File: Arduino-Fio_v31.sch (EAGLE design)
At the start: 56 parts, among them U1 MCP73831, U5 ATMEGA32U4, U6 MIC5219-3.3, X1 MJ4435-R1503_03, X2 USB_MICROB_PLUGCONN-11752, Y2 8MHz

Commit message: V 0.11 now with SD card slot
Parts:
- added U$3: MICROSD, adafruit:MICROSD
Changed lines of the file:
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@@
 <part name="PAD5" library="wirepad" deviceset="WIREPAD" device="SMD1,27-254"/>
 <part name="PAD6" library="wirepad" deviceset="WIREPAD" device="SMD1,27-254"/>
+<part name="U$3" library="adafruit" deviceset="MICROSD" device=""/>
 </parts>
 <sheets>
@@
 <instance part="PAD5" gate="G$1" x="-33.02" y="104.14"/>
 <instance part="PAD6" gate="G$1" x="-33.02" y="96.52"/>
+<instance part="U$3" gate="G$1" x="307.34" y="109.22"/>
 </instances>
 <busses>

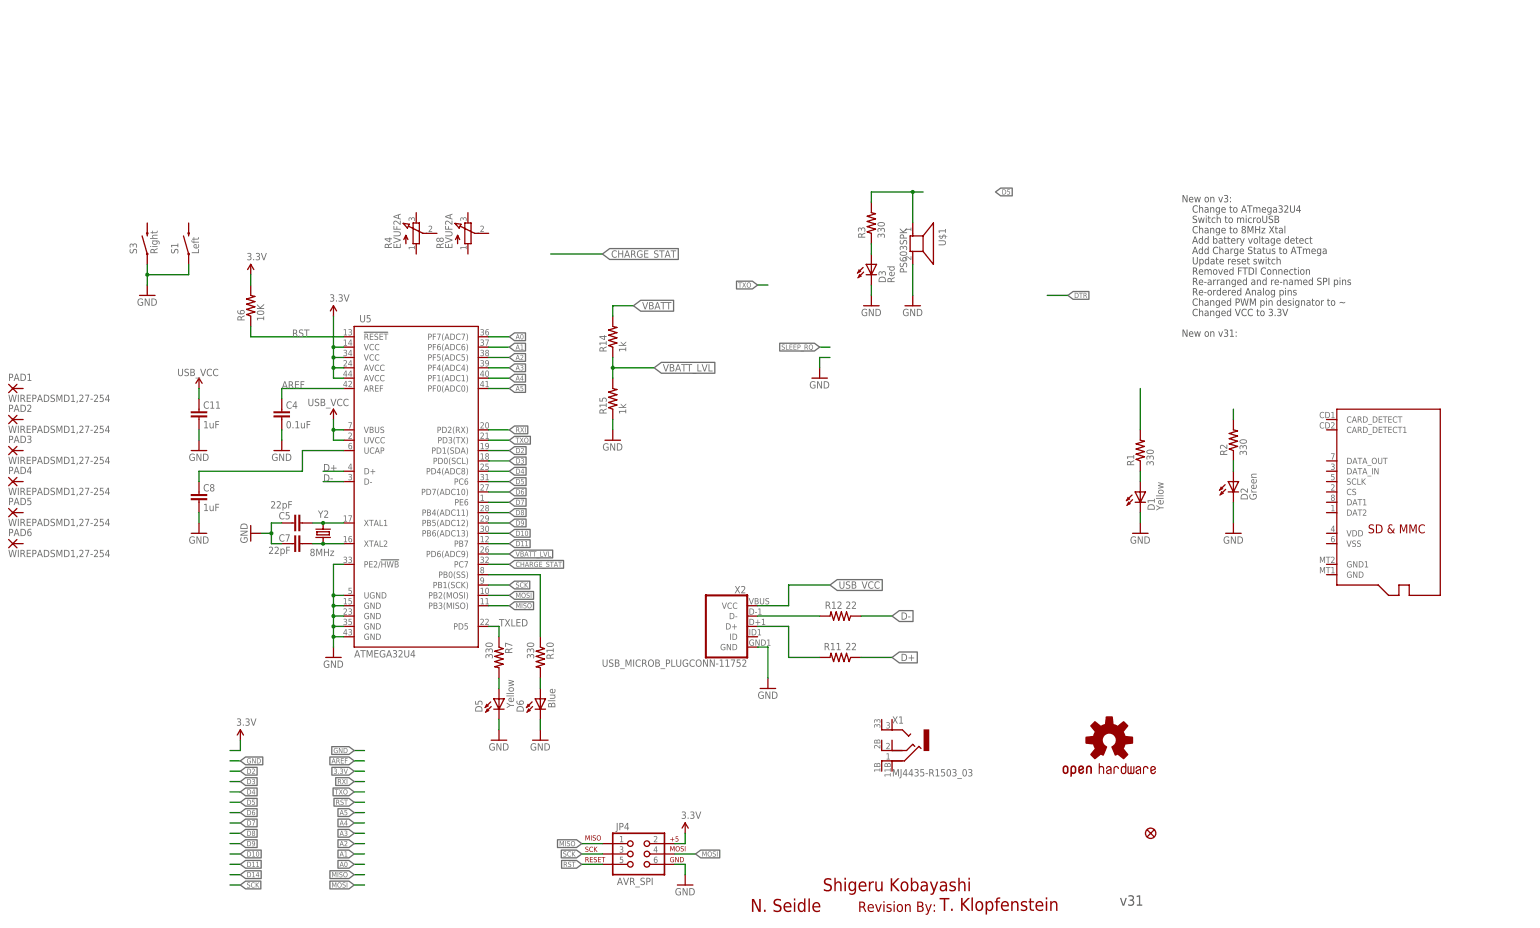
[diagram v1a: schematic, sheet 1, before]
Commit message: Finished Routing
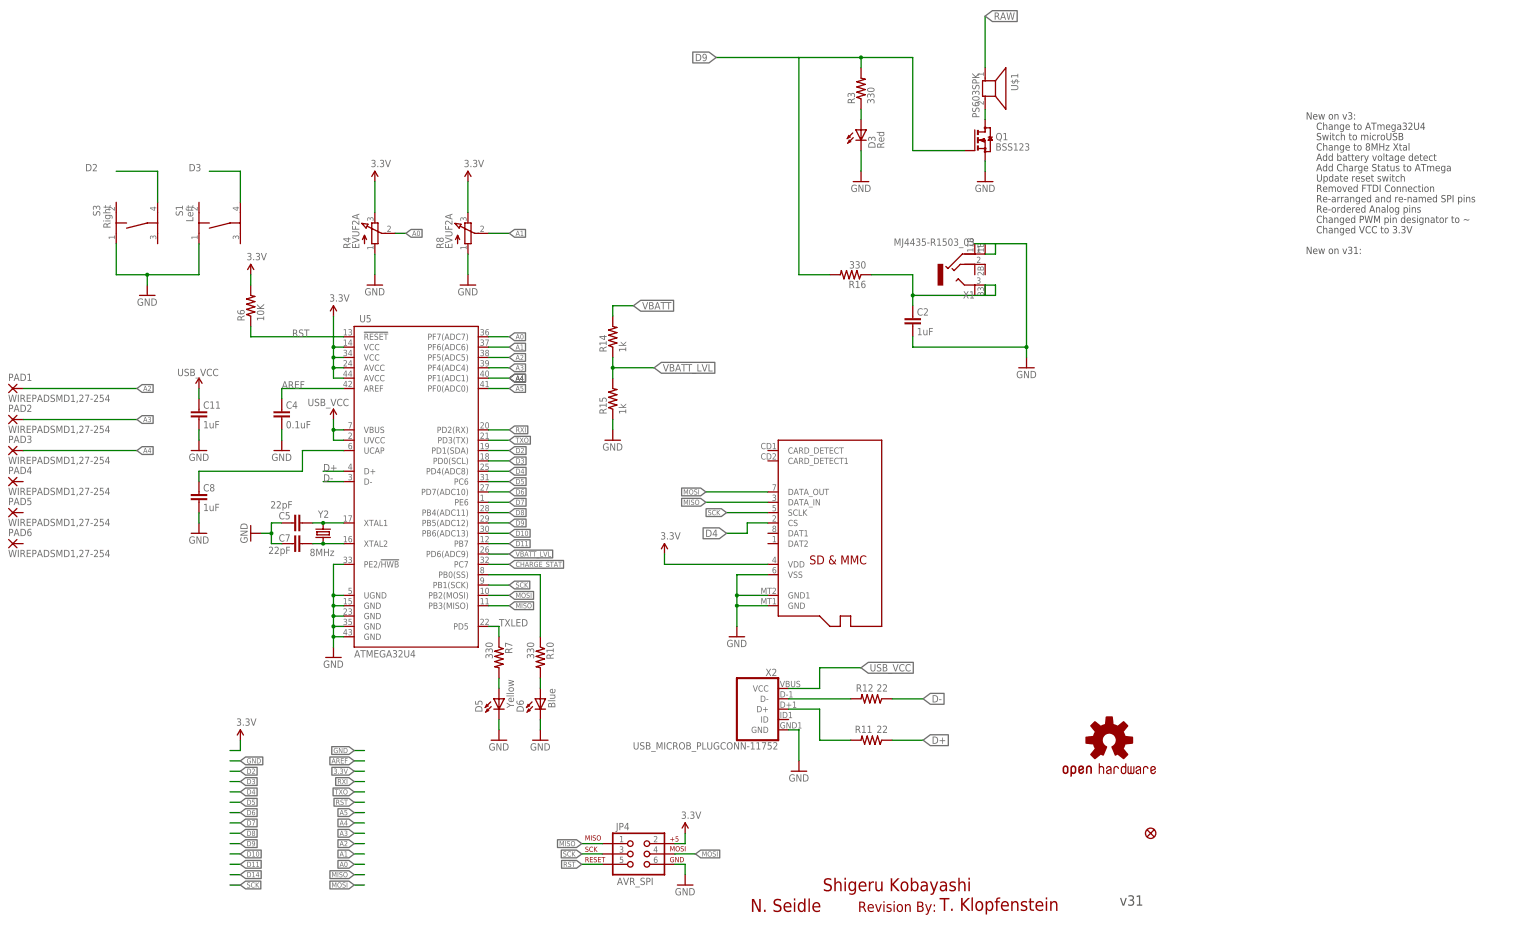
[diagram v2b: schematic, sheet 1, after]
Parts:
- removed D1: Yellow, SparkFun:LED0603
- removed D2: Green, SparkFun:LED0603
- removed R1, R2: 330, SparkFun-Resistors:RESISTOR0603-RES
- added C2: 1uF, SparkFun-Capacitors:CAP0603-CAP
- added Q1: BSS123, transistor-small-signal:BSS123
- added R16: 330, SparkFun-Resistors:RESISTOR0603-RES
- S1, S3: device SparkFun:SWITCH-MOMENTARY-2SMD -> Gaudi:TASTER-9314_SMD
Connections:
- removed net ASSOCIATE: R1.2
- removed net N$12: R3.2, U$1.1
- removed net N$2: D1.A, R1.1
- removed net N$3: D2.A, R2.1
- removed net N$4: R2.2
- new net N$13: Q1.D, U$1.2
- new net N$21: C2.2, R16.1, X1.3_1, X1.3_3, X1.3_4
- net 3.3V: now also R4.E, R8.E, U$3.VDD
- net A0: now also R4.S
- net A1: now also R8.S
- net A2: now also PAD1.P
- net A3: now also PAD2.P
- net A4: now also PAD3.P
- net D2: now also S3.4
- net D3: now also S1.4
- net D4: now also U$3.CS
- net D9: now also Q1.G, R16.2, R3.2
- net GND: now also C2.1, Q1.S, R4.A, R8.A, U$3.GND, U$3.GND1, U$3.VSS, X1.1_1, X1.1_3, X1.1_4; no longer D1.C, D2.C, U$1.2
- net MISO: now also U$3.DATA_IN
- net MOSI: now also U$3.DATA_OUT
- net RAW: now also U$1.1
- net SCK: now also U$3.SCLK
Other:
- moved on the sheet: D3, R11, R12, R3, R4, U$1, X1, X2
